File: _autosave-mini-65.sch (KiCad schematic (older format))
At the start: 175 parts, among them J1 TYPE-C-31-M12_13_EDITED, J2 AVR-ISP-6, SW1 SW_Push, U1 ATmega32U4-AU, U2 WE-TVS-82400102, Y1 Crystal_GND24_Small

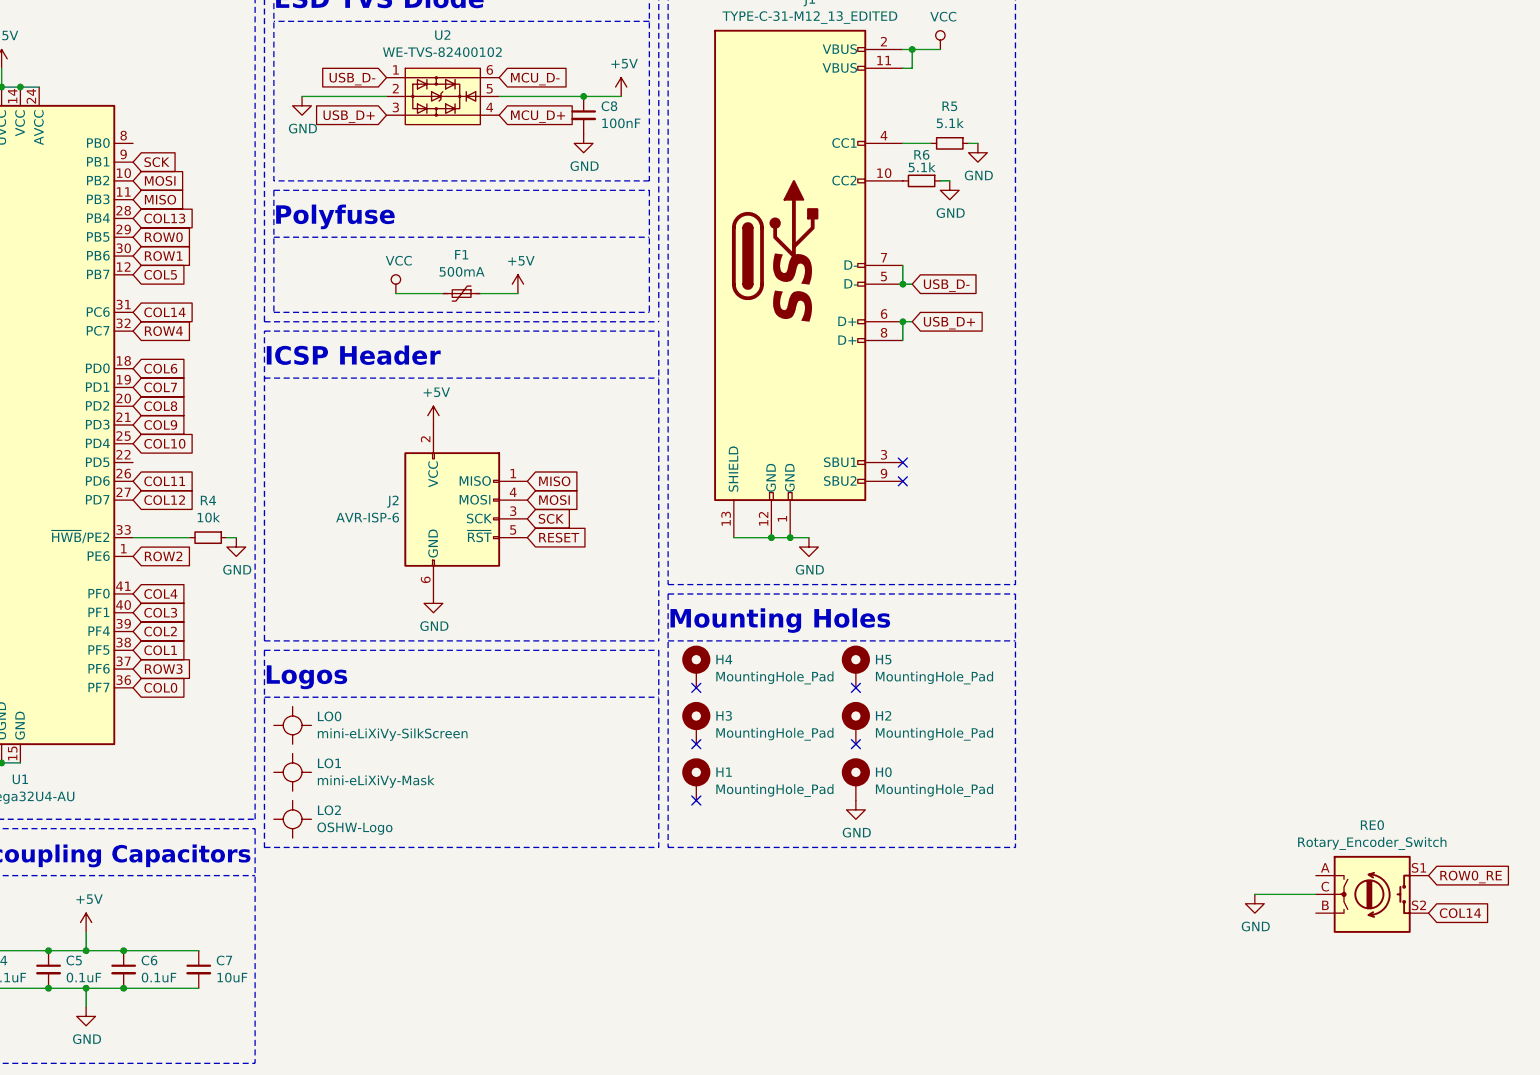
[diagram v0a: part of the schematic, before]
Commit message: Added rotary encoder first steps
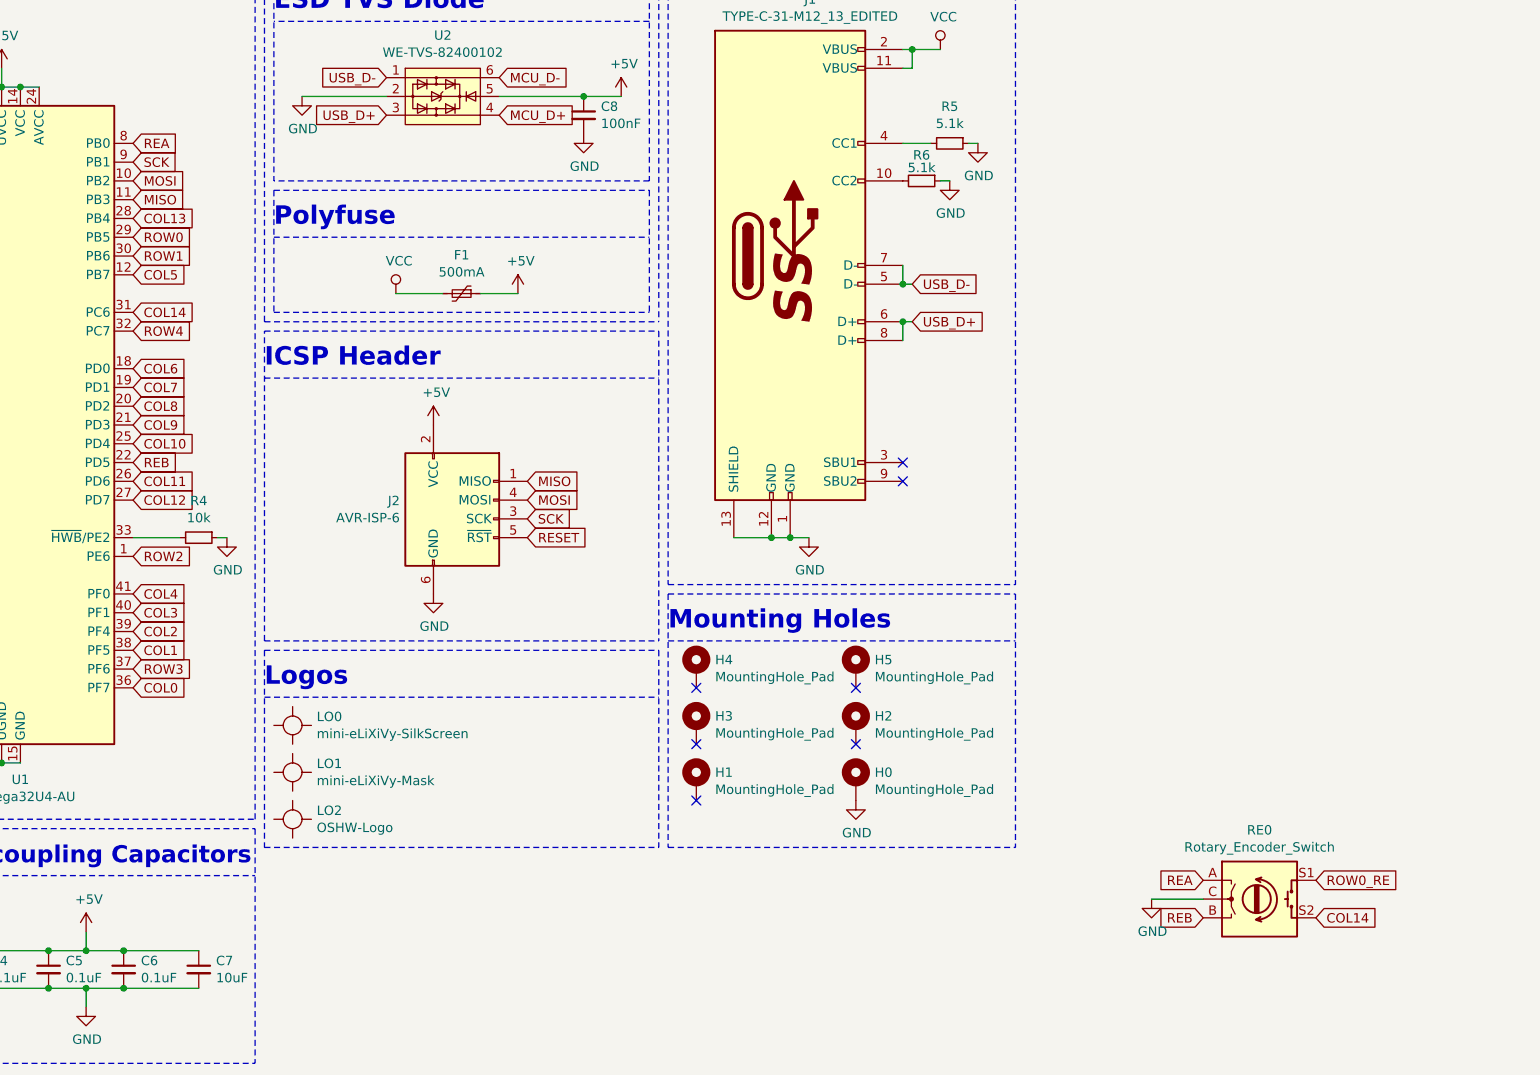
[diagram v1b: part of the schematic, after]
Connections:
- net REB: now reaches U1.22 (PD5)
- net REB: now also RE0.B
- net REA: now reaches U1.8 (PB0)
- net REA: now also RE0.A
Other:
- moved on the sheet: R4, RE0
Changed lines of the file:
@@
 Wire Wire Line
 	4750 4200 5325 4200
-Connection ~ 6275 4900
 Connection ~ 5725 4900
-Wire Wire Line
-	5725 4900 6275 4900
 Connection ~ 5325 4900
 Connection ~ 4750 4900
@@
 Wire Wire Line
 	3550 4200 3950 4200
-Wire Wire Line
-	6275 4900 6875 4900
 Wire Wire Line
 	6275 4200 6875 4200
@@
 	3850 3700 3850 4400
 Wire Wire Line
-	6875 4900 7275 4900
-Connection ~ 6875 4900
-Wire Wire Line
 	5325 4900 5725 4900
 Wire Wire Line
@@
 Wire Wire Line
 	900  2100 1100 2100
-Wire Wire Line
-	7175 3700 7175 4400
-Connection ~ 7175 3700
 Wire Wire Line
 	7175 2300 7175 3700
@@
 Wire Wire Line
 	7175 2300 7200 2300
-Wire Wire Line
-	6575 3700 6575 4400
-Connection ~ 6575 3700
 Wire Wire Line
 	6575 3000 6575 3700
@@
 $EndComp
 $Comp
-L Diode:1N4148W D68
-U 1 1 624EA389
-P 7275 4750
-F 0 "D68" H 7270 4663 50  0000 R CNN
-F 1 "1N4148W" H 7334 4608 28  0000 R CNN
-F 2 "mini-general-tweaks:D_SOD123_axial-dual" H 7275 4575 50  0001 C CNN
-F 3 "https://www.vishay.com/docs/85748/1n4148w.pdf" H 7275 4750 50  0001 C CNN
-	1    7275 4750
-	0    -1   -1   0
-$EndComp
-$Comp
-L Diode:1N4148W D67
-U 1 1 624DD549
-P 6875 4750
-F 0 "D67" H 6870 4663 50  0000 R CNN
-F 1 "1N4148W" H 6934 4608 28  0000 R CNN
-F 2 "mini-general-tweaks:D_SOD123_axial-dual" H 6875 4575 50  0001 C CNN
-F 3 "https://www.vishay.com/docs/85748/1n4148w.pdf" H 6875 4750 50  0001 C CNN
-	1    6875 4750
-	0    -1   -1   0
-$EndComp
-$Comp
-L Diode:1N4148W D66
-U 1 1 624D06BD
-P 6275 4750
-F 0 "D66" H 6270 4663 50  0000 R CNN
-F 1 "1N4148W" H 6334 4608 28  0000 R CNN
-F 2 "mini-general-tweaks:D_SOD123_axial-dual" H 6275 4575 50  0001 C CNN
-F 3 "https://www.vishay.com/docs/85748/1n4148w.pdf" H 6275 4750 50  0001 C CNN
-	1    6275 4750
-	0    -1   -1   0
-$EndComp
-$Comp
 L Diode:1N4148W D65
 U 1 1 624C36E1
@@
 	1250 3900 1250 3950
 Wire Wire Line
-	6975 4600 6875 4600
-$Comp
-L MX_Alps_Hybrid:MX-NoLED MX_ARR_D1
-U 1 1 5F474908
-P 7025 4450
-F 0 "MX_ARR_D1" H 6997 4624 30  0000 C CNN
-F 1 "MX-NoLED" H 6999 4569 20  0000 C CNN
-F 2 "mini-MX-Tweaks:MXOnly-1U-NoLED_tweak" H 6400 4425 60  0001 C CNN
-F 3 "" H 6400 4425 60  0001 C CNN
-	1    7025 4450
-	1    0    0    -1
-$EndComp
-Wire Wire Line
 	6975 2500 6875 2500
 $Comp
@@
 	7375 3900 7275 3900
 Wire Wire Line
-	7375 4600 7275 4600
-Wire Wire Line
 	7375 2500 7275 2500
 $Comp
@@
 $EndComp
 Connection ~ 6975 2500
-$Comp
-L MX_Alps_Hybrid:MX-NoLED MX_ARR_R1
-U 1 1 5F48B682
-P 7425 4450
-F 0 "MX_ARR_R1" H 7397 4624 30  0000 C CNN
-F 1 "MX-NoLED" H 7399 4569 20  0000 C CNN
-F 2 "mini-MX-Tweaks:MXOnly-1U-NoLED_tweak" H 6800 4425 60  0001 C CNN
-F 3 "" H 6800 4425 60  0001 C CNN
-	1    7425 4450
-	1    0    0    -1
-$EndComp
 Wire Wire Line
 	6975 3900 6875 3900
@@
 Wire Wire Line
 	6375 2500 6275 2500
-$Comp
-L MX_Alps_Hybrid:MX-NoLED MX_ARR_L1
-U 1 1 5F45D4BC
-P 6425 4450
-F 0 "MX_ARR_L1" H 6397 4624 30  0000 C CNN
-F 1 "MX-NoLED" H 6399 4569 20  0000 C CNN
-F 2 "mini-MX-Tweaks:MXOnly-1U-NoLED_tweak" H 5800 4425 60  0001 C CNN
-F 3 "" H 5800 4425 60  0001 C CNN
-	1    6425 4450
-	1    0    0    -1
-$EndComp
-Wire Wire Line
-	6375 4600 6275 4600
 $Comp
 L MX_Alps_Hybrid:MX-NoLED MX_1.75U_CAPSLOCK1
@@
 L power:GND #PWR0104
 U 1 1 5F16F0E0
-P 3400 8250
-F 0 "#PWR0104" H 3400 8000 50  0001 C CNN
-F 1 "GND" H 3405 8077 50  0000 C CNN
-F 2 "" H 3400 8250 50  0001 C CNN
-F 3 "" H 3400 8250 50  0001 C CNN
-	1    3400 8250
-	1    0    0    -1
-$EndComp
-Wire Wire Line
-	3350 8250 3400 8250
+P 3350 8250
+F 0 "#PWR0104" H 3350 8000 50  0001 C CNN
+F 1 "GND" H 3355 8077 50  0000 C CNN
+F 2 "" H 3350 8250 50  0001 C CNN
+F 3 "" H 3350 8250 50  0001 C CNN
+	1    3350 8250
+	1    0    0    -1
+$EndComp
+Wire Wire Line
+	3300 8250 3350 8250
 $Comp
 L Device:R_Small R4
 U 1 1 5F16CB52
-P 3250 8250
-F 0 "R4" V 3054 8250 50  0000 C CNN
-F 1 "10k" V 3145 8250 50  0000 C CNN
-F 2 "Resistor_SMD:R_0805_2012Metric" H 3250 8250 50  0001 C CNN
-F 3 "~" H 3250 8250 50  0001 C CNN
-	1    3250 8250
+P 3200 8250
+F 0 "R4" V 3004 8250 50  0000 C CNN
+F 1 "10k" V 3095 8250 50  0000 C CNN
+F 2 "Resistor_SMD:R_0805_2012Metric" H 3200 8250 50  0001 C CNN
+F 3 "~" H 3200 8250 50  0001 C CNN
+	1    3200 8250
 	0    1    1    0
 $EndComp
-Wire Wire Line
-	2850 8250 3150 8250
 $Comp
 L power:GND #PWR0106
@@
 Text GLabel 7275 1800 1    50   Input ~ 0
 ROW0_RE
-Text GLabel 9750 10050 2    50   Input ~ 0
+Text GLabel 9150 10075 2    50   Input ~ 0
 ROW0_RE
-Text GLabel 9750 10250 2    50   Input ~ 0
+Text GLabel 9150 10275 2    50   Input ~ 0
 COL14
 $Comp
 L power:GND #PWR0123
 U 1 1 64F8DD45
-P 8825 10150
-F 0 "#PWR0123" H 8825 9900 50  0001 C CNN
-F 1 "GND" H 8830 9977 50  0000 C CNN
-F 2 "" H 8825 10150 50  0001 C CNN
-F 3 "" H 8825 10150 50  0001 C CNN
-	1    8825 10150
-	1    0    0    -1
-$EndComp
-Wire Wire Line
-	8825 10150 9150 10150
+P 8275 10175
+F 0 "#PWR0123" H 8275 9925 50  0001 C CNN
+F 1 "GND" H 8280 10002 50  0000 C CNN
+F 2 "" H 8275 10175 50  0001 C CNN
+F 3 "" H 8275 10175 50  0001 C CNN
+	1    8275 10175
+	1    0    0    -1
+$EndComp
 $Comp
 L Device:Rotary_Encoder_Switch RE0
 U 1 1 64FB0777
-P 9450 10150
-F 0 "RE0" H 9450 10517 50  0000 C CNN
-F 1 "Rotary_Encoder_Switch" H 9450 10426 50  0000 C CNN
-F 2 "Rotary_Encoder:RotaryEncoder_Alps_EC11E-Switch_Vertical_H20mm_CircularMountingHoles" H 9300 10310 50  0001 C CNN
-F 3 "~" H 9450 10410 50  0001 C CNN
-	1    9450 10150
-	1    0    0    -1
-$EndComp
+P 8850 10175
+F 0 "RE0" H 8850 10542 50  0000 C CNN
+F 1 "Rotary_Encoder_Switch" H 8850 10451 50  0000 C CNN
+F 2 "Rotary_Encoder:RotaryEncoder_Alps_EC11E-Switch_Vertical_H20mm_CircularMountingHoles" H 8700 10335 50  0001 C CNN
+F 3 "~" H 8850 10435 50  0001 C CNN
+	1    8850 10175
+	1    0    0    -1
+$EndComp
+Wire Wire Line
+	2850 8250 3100 8250
+Connection ~ 6575 3700
+Connection ~ 7175 3700
+Connection ~ 6875 4900
+Wire Wire Line
+	6875 4900 7275 4900
+Wire Wire Line
+	6275 4900 6875 4900
+Wire Wire Line
+	5725 4900 6275 4900
+Connection ~ 6275 4900
+Wire Wire Line
+	6375 4600 6275 4600
+$Comp
+L MX_Alps_Hybrid:MX-NoLED MX_ARR_L1
+U 1 1 5F45D4BC
+P 6425 4450
+F 0 "MX_ARR_L1" H 6397 4624 30  0000 C CNN
+F 1 "MX-NoLED" H 6399 4569 20  0000 C CNN
+F 2 "mini-MX-Tweaks:MXOnly-1U-NoLED_tweak" H 5800 4425 60  0001 C CNN
+F 3 "" H 5800 4425 60  0001 C CNN
+	1    6425 4450
+	1    0    0    -1
+$EndComp
+$Comp
+L MX_Alps_Hybrid:MX-NoLED MX_ARR_R1
+U 1 1 5F48B682
+P 7425 4450
+F 0 "MX_ARR_R1" H 7397 4624 30  0000 C CNN
+F 1 "MX-NoLED" H 7399 4569 20  0000 C CNN
+F 2 "mini-MX-Tweaks:MXOnly-1U-NoLED_tweak" H 6800 4425 60  0001 C CNN
+F 3 "" H 6800 4425 60  0001 C CNN
+	1    7425 4450
+	1    0    0    -1
+$EndComp
+Wire Wire Line
+	7375 4600 7275 4600
+$Comp
+L MX_Alps_Hybrid:MX-NoLED MX_ARR_D1
+U 1 1 5F474908
+P 7025 4450
+F 0 "MX_ARR_D1" H 6997 4624 30  0000 C CNN
+F 1 "MX-NoLED" H 6999 4569 20  0000 C CNN
+F 2 "mini-MX-Tweaks:MXOnly-1U-NoLED_tweak" H 6400 4425 60  0001 C CNN
+F 3 "" H 6400 4425 60  0001 C CNN
+	1    7025 4450
+	1    0    0    -1
+$EndComp
+Wire Wire Line
+	6975 4600 6875 4600
+$Comp
+L Diode:1N4148W D66
+U 1 1 624D06BD
+P 6275 4750
+F 0 "D66" H 6270 4663 50  0000 R CNN
+F 1 "1N4148W" H 6334 4608 28  0000 R CNN
+F 2 "mini-general-tweaks:D_SOD123_axial-dual" H 6275 4575 50  0001 C CNN
+F 3 "https://www.vishay.com/docs/85748/1n4148w.pdf" H 6275 4750 50  0001 C CNN
+	1    6275 4750
+	0    -1   -1   0
+$EndComp
+$Comp
+L Diode:1N4148W D67
+U 1 1 624DD549
+P 6875 4750
+F 0 "D67" H 6870 4663 50  0000 R CNN
+F 1 "1N4148W" H 6934 4608 28  0000 R CNN
+F 2 "mini-general-tweaks:D_SOD123_axial-dual" H 6875 4575 50  0001 C CNN
+F 3 "https://www.vishay.com/docs/85748/1n4148w.pdf" H 6875 4750 50  0001 C CNN
+	1    6875 4750
+	0    -1   -1   0
+$EndComp
+$Comp
+L Diode:1N4148W D68
+U 1 1 624EA389
+P 7275 4750
+F 0 "D68" H 7270 4663 50  0000 R CNN
+F 1 "1N4148W" H 7334 4608 28  0000 R CNN
+F 2 "mini-general-tweaks:D_SOD123_axial-dual" H 7275 4575 50  0001 C CNN
+F 3 "https://www.vishay.com/docs/85748/1n4148w.pdf" H 7275 4750 50  0001 C CNN
+	1    7275 4750
+	0    -1   -1   0
+$EndComp
+Wire Wire Line
+	6575 3700 6575 4400
+Wire Wire Line
+	7175 3700 7175 4400
+Text GLabel 2850 6150 2    50   Input ~ 0
+REA
+Text GLabel 2850 7850 2    50   Input ~ 0
+REB
+Text GLabel 8550 10075 0    50   Input ~ 0
+REA
+Text GLabel 8550 10275 0    50   Input ~ 0
+REB
+Wire Wire Line
+	8275 10175 8550 10175
 $EndSCHEMATC
